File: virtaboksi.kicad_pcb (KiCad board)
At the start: 2 copper layers, 50 x 72 mm, 64 parts, among them J1 Panel_01x06, J2 External_01x06, J3 Optional_01x03, J5 Powerpole 01x02, J6 Powerpole 01x02, J7 Powerpole 01x02, J8 TagConnect_TC2030-NL, Q1 2N7002, Q2 IRF4905, Q3 IRF4905, Q4 2N7002, Q5 IRF4905, Q6 IRF4905, Q7 2N7002, Q8 IRF4905, Q9 IRF4905, U1 SRV05-4, U2 AMSRI-783.3-NZ, U3 SRV05-4, U4 SP3485EN, U5 STM8S003F3P

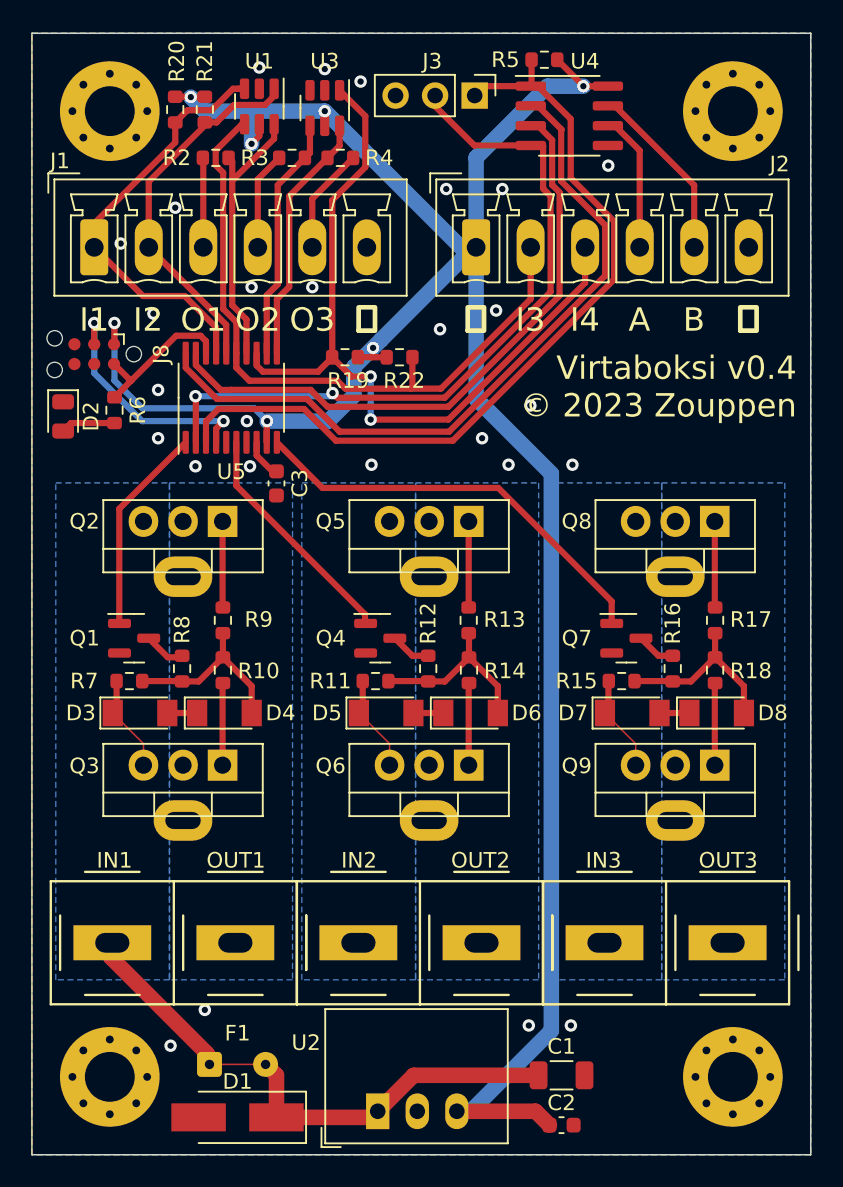
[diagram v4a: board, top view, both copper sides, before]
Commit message: Add current mirror, rename traces
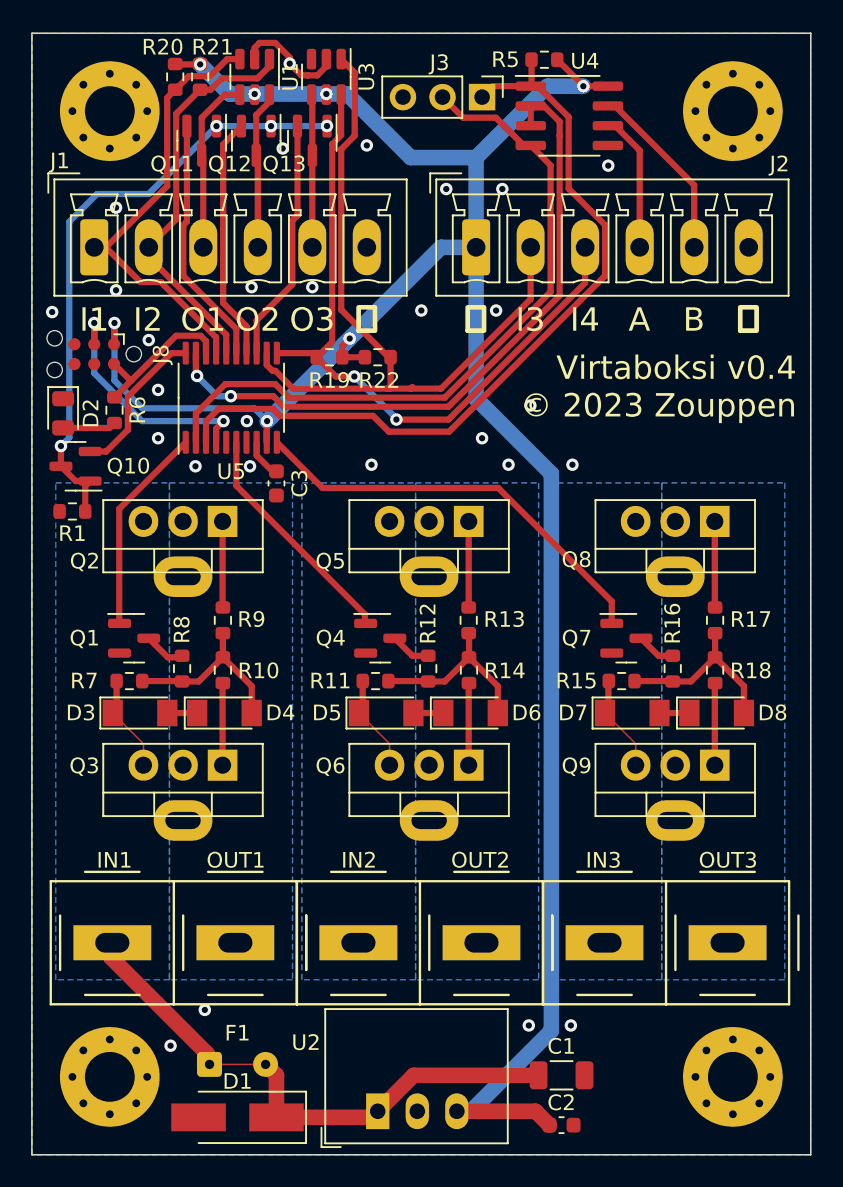
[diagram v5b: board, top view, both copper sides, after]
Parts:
- removed R2, R3, R4: 180, Resistor_SMD:R_0603_1608Metric
- added Q10: MMBT3906, Package_TO_SOT_SMD:SOT-23, F.Cu at (108.8, 62.8)
- added Q11: MMBT3906, Package_TO_SOT_SMD:SOT-23, F.Cu at (116.9, 41.9)
- added Q12: MMBT3906, Package_TO_SOT_SMD:SOT-23, F.Cu at (120.4, 41.9)
- added Q13: MMBT3906, Package_TO_SOT_SMD:SOT-23, F.Cu at (124.0, 41.9)
- added R1: 180, Resistor_SMD:R_0603_1608Metric, F.Cu at (108.6, 65.7)
- moved R21 2.12 mm to (116.8, 37.8)
- moved R20 2.10 mm to (115.2, 37.8)
- moved U3 2.00 mm to (124.9, 37.8)
- moved U1 1.92 mm to (120.3, 37.8)
- moved R22 1.40 mm to (128.2, 55.8)
- moved R19 1.00 mm to (125.1, 55.8)
- moved J3 0.49 mm to (134.9, 39.1)
- moved D2 0.20 mm to (108.0, 59.4)
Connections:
- J1 pad 3: Net-(J1-Pad3) -> /O1
- J1 pad 4: Net-(J1-Pad4) -> /O2
- J1 pad 5: Net-(J1-Pad5) -> /O3
- U1 pad 4: /IN3 -> /O1
- U1 pad 6: /LED1 -> /O2
- U3 pad 1: /IN4 -> /IN3
- U3 pad 4: /LED2 -> /O3
- U3 pad 6: /LED3 -> /IN4
- U4 pad 2: /TX_EN1 -> /TX_EN
- U4 pad 3: /TX_EN2 -> /TX_EN
- U5 pad 11: /LED3 -> /IN4
- U5 pad 12: /LED2 -> /IN3
- U5 pad 13: /IN4 -> /O3INT
- U5 pad 14: /LED1 -> /O2INT
- U5 pad 15: /IN3 -> /O1INT
- U5 pad 19: /TX_EN2 -> /TX_EN
- U5 pad 20: /TX_EN1 -> /IREF_EN
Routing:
- net /TX_EN1: track 47.2 -> 0.00 mm
- net /TX_EN: track 0.00 -> 43.3 mm, vias 0 -> 2
- net /TX_EN2: track 40.1 -> 0.00 mm
- net /IREF: track 0.00 -> 39.6 mm, vias 0 -> 4
- net /LED1: track 17.8 -> 0.00 mm
- net /LED3: track 16.3 -> 0.00 mm
- net /O1INT: track 0.00 -> 16.1 mm
- net /LED2: track 15.7 -> 0.00 mm
- net /O2INT: track 0.00 -> 15.7 mm
- net /O3INT: track 0.00 -> 15.7 mm
- net /O1: track 0.00 -> 11.4 mm
- net /O2: track 0.00 -> 10.2 mm
- net /IREF_EN: track 0.00 -> 10.00 mm
- net /O3: track 0.00 -> 9.83 mm
- net +3.3V: track 154.0 -> 146.7 mm
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
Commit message: Move vias off the SMD pads
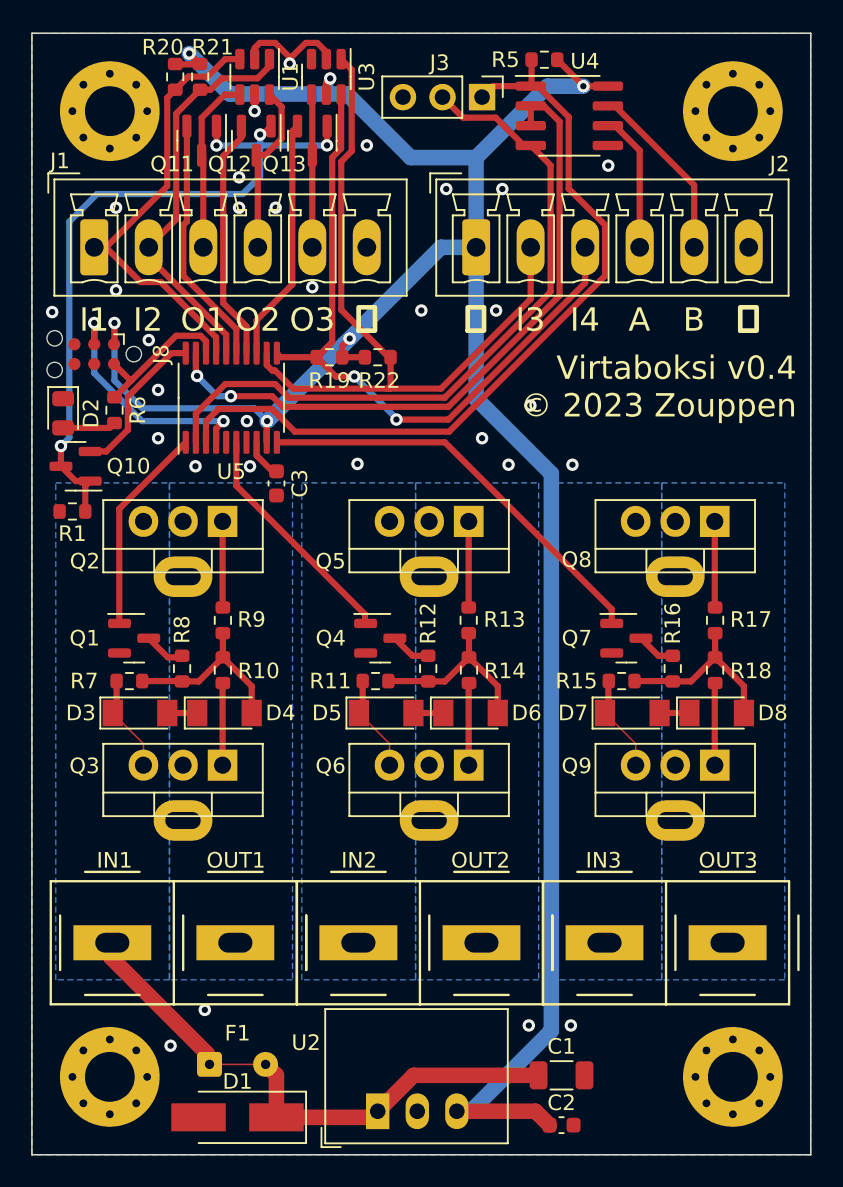
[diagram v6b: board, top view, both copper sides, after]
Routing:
- net /IREF: track 39.6 -> 46.9 mm
- net +3.3V: track 146.7 -> 152.2 mm
- net /O2: track 10.2 -> 11.1 mm
- net GND: track 7.22 -> 8.09 mm, vias 28 -> 29

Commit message: Approach version 0.5. Let it cool down for day or two.
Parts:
- moved C3 1.06 mm to (122.5, 63.1), turned to 0 degrees
- moved R1 0.87 mm to (107.8, 66.2), turned to -90 degrees
- moved Q10 0.25 mm to (109.0, 62.8)
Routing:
- net +3.3V: track 152.2 -> 151.6 mm
- net GND: track 8.09 -> 7.94 mm, vias 29 -> 30

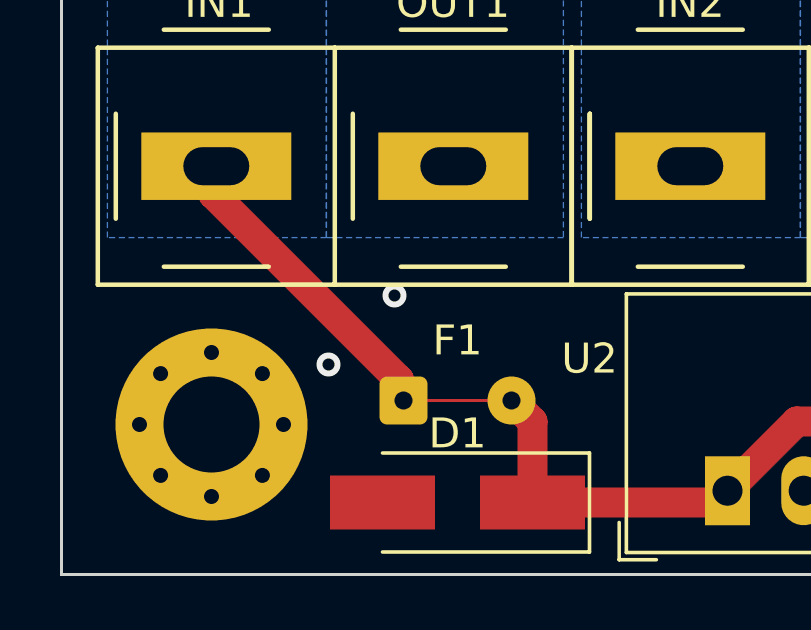
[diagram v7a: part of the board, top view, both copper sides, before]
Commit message: Remove one unnecessary via
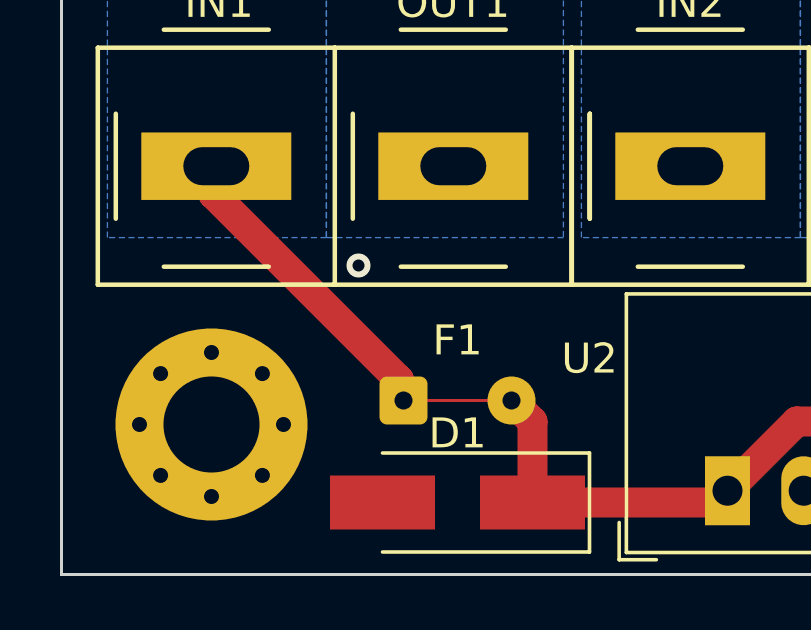
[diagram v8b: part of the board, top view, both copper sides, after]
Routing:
- net GND: vias 30 -> 29
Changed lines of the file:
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@@
   (via (at 134.9 61) (size 0.8) (drill 0.4) (layers "F.Cu" "B.Cu") (free) (net 1))
   (via (at 113.5 54.7) (size 0.8) (drill 0.4) (layers "F.Cu" "B.Cu") (free) (net 1))
-  (via (at 114.9 100) (size 0.8) (drill 0.4) (layers "F.Cu" "B.Cu") (free) (net 1))
   (via (at 138 97) (size 0.8) (drill 0.4) (layers "F.Cu" "B.Cu") (free) (net 1))
   (via (at 120 62.8) (size 0.8) (drill 0.4) (layers "F.Cu" "B.Cu") (free) (net 1))
@@
   (via (at 119.3 46.2) (size 0.8) (drill 0.4) (layers "F.Cu" "B.Cu") (free) (net 1))
   (via (at 114.1 57.9) (size 0.8) (drill 0.4) (layers "F.Cu" "B.Cu") (free) (net 1))
-  (via (at 117.1 97.7) (size 0.8) (drill 0.4) (layers "F.Cu" "B.Cu") (free) (net 1))
+  (via (at 115.9 96.7) (size 0.8) (drill 0.4) (layers "F.Cu" "B.Cu") (free) (net 1))
   (via (at 111.4 51.5) (size 0.8) (drill 0.4) (layers "F.Cu" "B.Cu") (free) (net 1))
   (via (at 111.4 46.2) (size 0.8) (drill 0.4) (layers "F.Cu" "B.Cu") (free) (net 1))
